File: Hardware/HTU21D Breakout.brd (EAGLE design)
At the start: 15.2 x 15.2 mm, 13 parts, among them U1 HTU21D

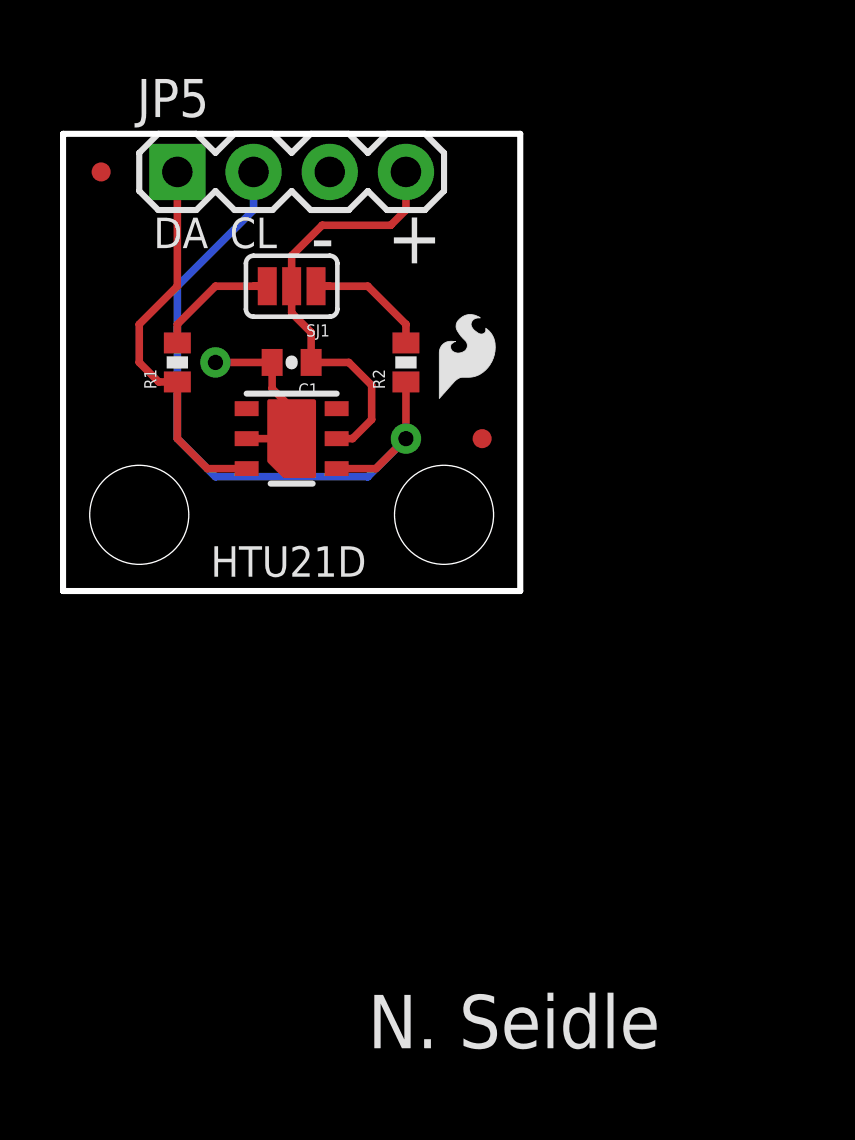
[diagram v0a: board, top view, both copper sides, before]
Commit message: Re-routing post review with engineering recommendations.
Moved to 0603 footprints. Removed ground planes to align with datasheet
thermal recommendations. Added OSHW logo. Updated frame to CC 3.0. Added
revision code to bottom copper.
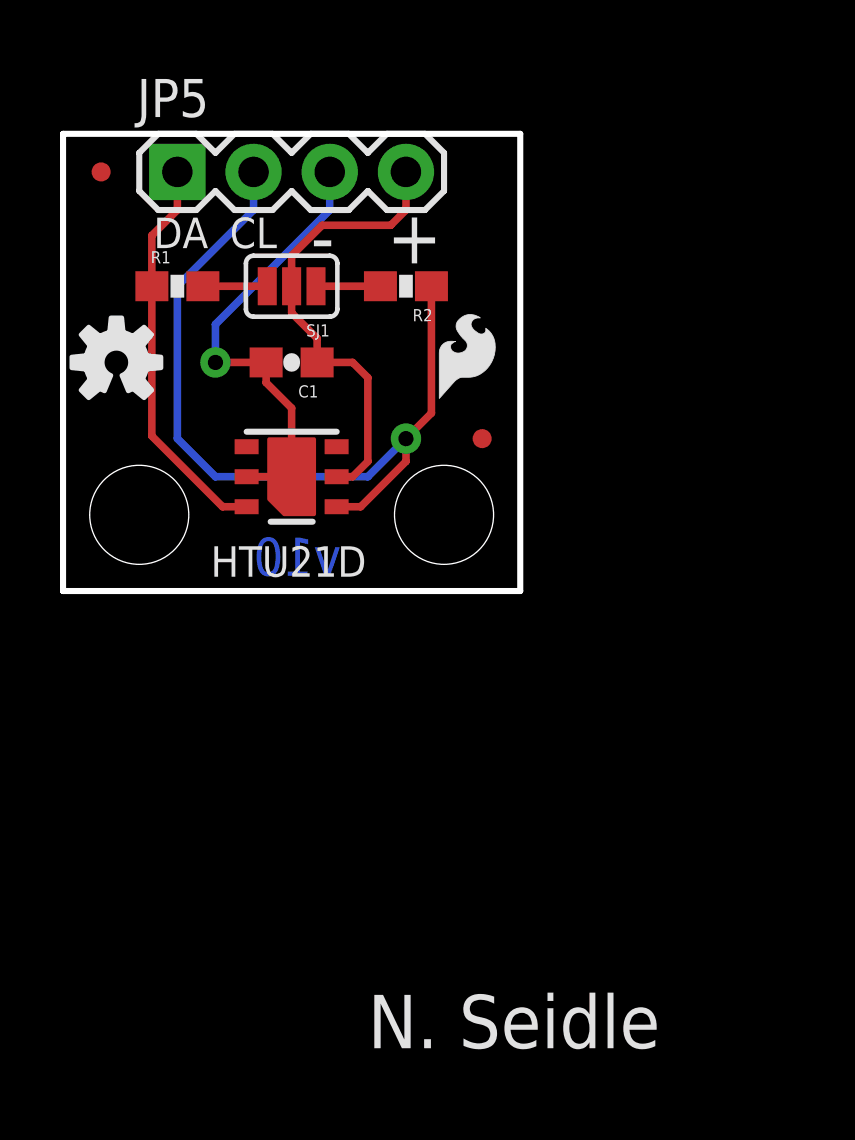
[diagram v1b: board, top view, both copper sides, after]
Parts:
- removed FRAME1: FRAME-LETTER, SparkFun-Aesthetics:CREATIVE_COMMONS
- added FRAME2: FRAME-LETTER, SparkFun-Aesthetics:CREATIVE_COMMONS
- added LOGO2: OSHW-LOGOS, SparkFun-Aesthetics:OSHW-LOGO-S
- C1: device SparkFun:0402-CAP -> SparkFun:0603-CAP
- R1, R2: device SparkFun:0402-RES -> SparkFun:0603-RES
- moved R1 2.54 mm to (3.81, 10.2), turned to 0 degrees
- moved R2 2.54 mm to (11.4, 10.2), turned to 180 degrees
- moved U1 1.27 mm to (7.62, 3.81)
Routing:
- net GND: track 6.20 -> 15.3 mm
- net SCL: track 23.2 -> 27.7 mm
- net N$1: track 4.60 -> 2.15 mm
- net N$2: track 4.60 -> 2.15 mm
- net 3.3V: track 14.4 -> 15.6 mm
- removed copper zone on layer 1, net GND
- removed copper zone on layer 16, net GND
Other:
- board text added: "v10"
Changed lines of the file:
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@@
 <?xml version="1.0" encoding="utf-8"?>
 <!DOCTYPE eagle SYSTEM "eagle.dtd">
-<eagle version="6.5.0">
+<eagle version="6.4">
 <drawing>
 <settings>
@@
 <text x="3.01625" y="11.43" size="1.016" layer="21" font="vector" ratio="15">DA</text>
 <text x="10.16" y="-15.24" size="1.778" layer="21">N. Seidle</text>
+<text x="9.271" y="0.508" size="1.27" layer="16" ratio="20" rot="MR0">v10</text>
 </plain>
 <attributes>
@@
 <elements>
 <element name="LOGO1" library="SparkFun" package="SFE-LOGO-FLAME" value="LOGO-SFESK" x="12.54125" y="6.4135"/>
-<element name="C1" library="SparkFun" package="0402-CAP" value="0.1uF" x="7.62" y="7.62" rot="R180"/>
-<element name="R1" library="SparkFun" package="0402-RES" value="4.7k" x="3.81" y="7.62" rot="R90"/>
-<element name="R2" library="SparkFun" package="0402-RES" value="4.7k" x="11.43" y="7.62" rot="R90"/>
+<element name="C1" library="SparkFun" package="0603-CAP" value="0.1uF" x="7.62" y="7.62" rot="R180"/>
+<element name="R1" library="SparkFun" package="0603-RES" value="4.7k" x="3.81" y="10.16"/>
+<element name="R2" library="SparkFun" package="0603-RES" value="4.7k" x="11.43" y="10.16" rot="R180"/>
 <element name="SJ1" library="mike-temp" package="SJ_3_PASTE1&amp;2&amp;3" value="" x="7.62" y="10.16" rot="R180"/>
 <element name="STANDOFF2" library="SparkFun-Electromechanical" package="STAND-OFF" value="STAND-OFF" x="2.54" y="2.54"/>
@@
 <element name="JP3" library="SparkFun-Aesthetics" package="MICRO-FIDUCIAL" value="FIDUCIALUFIDUCIAL" x="1.27" y="13.97"/>
 <element name="JP4" library="SparkFun-Aesthetics" package="MICRO-FIDUCIAL" value="FIDUCIALUFIDUCIAL" x="13.97" y="5.08"/>
-<element name="U1" library="SparkFun-Sensors" package="HTU21D" value="HTU21D" x="7.62" y="5.08"/>
-<element name="FRAME1" library="SparkFun-Aesthetics" package="CREATIVE_COMMONS" value="FRAME-LETTER" x="-22.6395375" y="-15.24"/>
+<element name="U1" library="SparkFun-Sensors" package="HTU21D" value="HTU21D" x="7.62" y="3.81"/>
 <element name="JP5" library="SparkFun-Connectors" package="1X04" value="" x="3.81" y="13.97"/>
+<element name="LOGO2" library="SparkFun-Aesthetics" package="OSHW-LOGO-S" value="OSHW-LOGOS" x="1.778" y="7.62"/>
+<element name="FRAME2" library="SparkFun-Aesthetics" package="CREATIVE_COMMONS" value="FRAME-LETTER" x="-21.59" y="-24.13"/>
 </elements>
 <signals>
 <signal name="GND">
 <contactref element="C1" pad="2"/>
-<polygon width="0.254" layer="1" isolate="0.254" orphans="yes">
-<vertex x="0" y="15.24"/>
-<vertex x="0" y="0"/>
-<vertex x="15.24" y="0"/>
-<vertex x="15.24" y="15.24"/>
-</polygon>
-<polygon width="0.254" layer="16" isolate="0.254" orphans="yes">
-<vertex x="0" y="15.24"/>
-<vertex x="0" y="0"/>
-<vertex x="15.24" y="0"/>
-<vertex x="15.24" y="15.24"/>
-</polygon>
 <contactref element="U1" pad="2"/>
 <contactref element="U1" pad="7"/>
@@
 <contactref element="U1" pad="2"/>
 <contactref element="JP5" pad="3"/>
-<wire x1="6.12" y1="5.08" x2="7.62" y2="5.08" width="0.254" layer="1"/>
-<wire x1="7.62" y1="5.08" x2="7.62" y2="6.096" width="0.254" layer="1"/>
-<wire x1="7.62" y1="6.096" x2="6.97" y2="6.746" width="0.254" layer="1"/>
-<wire x1="6.97" y1="7.62" x2="6.97" y2="6.746" width="0.254" layer="1"/>
-<wire x1="6.97" y1="7.62" x2="5.08" y2="7.62" width="0.254" layer="1"/>
+<wire x1="6.77" y1="7.62" x2="6.77" y2="6.946" width="0.254" layer="1"/>
 <via x="5.08" y="7.62" extent="1-16" drill="0.508"/>
+<wire x1="6.12" y1="3.81" x2="7.62" y2="3.81" width="0.254" layer="1"/>
+<wire x1="5.08" y1="7.62" x2="6.77" y2="7.62" width="0.254" layer="1"/>
+<wire x1="5.08" y1="8.89" x2="5.08" y2="7.62" width="0.254" layer="16"/>
+<wire x1="8.89" y1="13.97" x2="8.89" y2="12.7" width="0.254" layer="16"/>
+<wire x1="8.89" y1="12.7" x2="5.08" y2="8.89" width="0.254" layer="16"/>
+<wire x1="6.77" y1="6.946" x2="7.62" y2="6.096" width="0.254" layer="1"/>
+<wire x1="7.62" y1="6.096" x2="7.62" y2="3.81" width="0.254" layer="1"/>
 </signal>
 <signal name="SCL">
@@
 <contactref element="U1" pad="4"/>
 <contactref element="JP5" pad="2"/>
-<wire x1="9.12" y1="4.08" x2="10.43" y2="4.08" width="0.254" layer="1"/>
 <wire x1="6.35" y1="13.97" x2="6.35" y2="12.7" width="0.254" layer="16"/>
 <wire x1="6.35" y1="12.7" x2="3.81" y2="10.16" width="0.254" layer="16"/>
@@
 <wire x1="10.16" y1="3.81" x2="11.43" y2="5.08" width="0.254" layer="16"/>
 <via x="11.43" y="5.08" extent="1-16" drill="0.508"/>
-<wire x1="11.43" y1="6.97" x2="11.43" y2="5.08" width="0.254" layer="1"/>
-<wire x1="10.43" y1="4.08" x2="11.43" y2="5.08" width="0.254" layer="1"/>
+<wire x1="12.28" y1="10.16" x2="12.28" y2="5.93" width="0.254" layer="1"/>
+<wire x1="12.28" y1="5.93" x2="11.43" y2="5.08" width="0.254" layer="1"/>
+<wire x1="9.12" y1="2.81" x2="9.922" y2="2.81" width="0.254" layer="1"/>
+<wire x1="9.922" y1="2.81" x2="11.43" y2="4.318" width="0.254" layer="1"/>
+<wire x1="11.43" y1="4.318" x2="11.43" y2="5.08" width="0.254" layer="1"/>
 </signal>
 <signal name="SDA">
@@
 <contactref element="U1" pad="3"/>
 <contactref element="JP5" pad="1"/>
-<wire x1="6.12" y1="4.08" x2="4.81" y2="4.08" width="0.254" layer="1"/>
-<wire x1="3.81" y1="13.97" x2="3.81" y2="10.16" width="0.254" layer="1"/>
-<wire x1="3.81" y1="10.16" x2="2.54" y2="8.89" width="0.254" layer="1"/>
-<wire x1="2.54" y1="8.89" x2="2.54" y2="7.62" width="0.254" layer="1"/>
-<wire x1="3.81" y1="6.97" x2="3.19" y2="6.97" width="0.254" layer="1"/>
-<wire x1="3.19" y1="6.97" x2="2.54" y2="7.62" width="0.254" layer="1"/>
-<wire x1="3.81" y1="6.97" x2="3.81" y2="5.08" width="0.254" layer="1"/>
-<wire x1="4.81" y1="4.08" x2="3.81" y2="5.08" width="0.254" layer="1"/>
+<wire x1="2.96" y1="10.16" x2="2.96" y2="11.85" width="0.254" layer="1"/>
+<wire x1="2.96" y1="11.85" x2="3.81" y2="12.7" width="0.254" layer="1"/>
+<wire x1="3.81" y1="12.7" x2="3.81" y2="13.97" width="0.254" layer="1"/>
+<wire x1="2.96" y1="10.16" x2="2.96" y2="5.168" width="0.254" layer="1"/>
+<wire x1="6.12" y1="2.81" x2="5.318" y2="2.81" width="0.254" layer="1"/>
+<wire x1="5.318" y1="2.81" x2="2.96" y2="5.168" width="0.254" layer="1"/>
 </signal>
 <signal name="3.3V">
@@
 <contactref element="SJ1" pad="2"/>
 <contactref element="U1" pad="5"/>
-<wire x1="9.12" y1="5.08" x2="9.652" y2="5.08" width="0.254" layer="1"/>
-<wire x1="9.652" y1="5.08" x2="10.287" y2="5.715" width="0.254" layer="1"/>
-<wire x1="10.287" y1="5.715" x2="10.287" y2="6.858" width="0.254" layer="1"/>
-<wire x1="10.287" y1="6.858" x2="9.525" y2="7.62" width="0.254" layer="1"/>
-<wire x1="9.525" y1="7.62" x2="8.27" y2="7.62" width="0.254" layer="1"/>
-<wire x1="7.62" y1="10.16" x2="7.62" y2="9.271" width="0.254" layer="1"/>
-<wire x1="7.62" y1="9.271" x2="8.27" y2="8.621" width="0.254" layer="1"/>
-<wire x1="8.27" y1="7.62" x2="8.27" y2="8.621" width="0.254" layer="1"/>
 <wire x1="7.62" y1="10.16" x2="7.62" y2="11.176" width="0.254" layer="1"/>
 <wire x1="7.62" y1="11.176" x2="8.636" y2="12.192" width="0.254" layer="1"/>
@@
 <contactref element="JP5" pad="4"/>
 <wire x1="11.43" y1="13.97" x2="11.43" y2="12.7" width="0.254" layer="1"/>
+<wire x1="7.62" y1="10.16" x2="7.62" y2="9.271" width="0.254" layer="1"/>
+<wire x1="7.62" y1="9.271" x2="8.47" y2="8.421" width="0.254" layer="1"/>
+<wire x1="8.47" y1="7.62" x2="8.47" y2="8.421" width="0.254" layer="1"/>
+<wire x1="9.12" y1="3.81" x2="9.652" y2="3.81" width="0.254" layer="1"/>
+<wire x1="9.652" y1="3.81" x2="10.16" y2="4.318" width="0.254" layer="1"/>
+<wire x1="10.16" y1="4.318" x2="10.16" y2="7.112" width="0.254" layer="1"/>
+<wire x1="8.47" y1="7.62" x2="9.652" y2="7.62" width="0.254" layer="1"/>
+<wire x1="9.652" y1="7.62" x2="10.16" y2="7.112" width="0.254" layer="1"/>
 </signal>
 <signal name="N$1">
 <contactref element="R1" pad="2"/>
 <contactref element="SJ1" pad="3"/>
-<wire x1="6.8072" y1="10.16" x2="6.35" y2="10.16" width="0.254" layer="1"/>
-<wire x1="3.81" y1="8.89" x2="3.81" y2="8.27" width="0.254" layer="1"/>
-<wire x1="3.81" y1="8.89" x2="5.08" y2="10.16" width="0.254" layer="1"/>
-<wire x1="5.08" y1="10.16" x2="6.8072" y2="10.16" width="0.254" layer="1"/>
+<wire x1="4.66" y1="10.16" x2="6.8072" y2="10.16" width="0.254" layer="1"/>
 </signal>
 <signal name="N$2">
 <contactref element="R2" pad="2"/>
 <contactref element="SJ1" pad="1"/>
-<wire x1="8.4328" y1="10.16" x2="8.89" y2="10.16" width="0.254" layer="1"/>
-<wire x1="11.43" y1="8.89" x2="11.43" y2="8.27" width="0.254" layer="1"/>
-<wire x1="11.43" y1="8.89" x2="10.16" y2="10.16" width="0.254" layer="1"/>
-<wire x1="10.16" y1="10.16" x2="8.4328" y2="10.16" width="0.254" layer="1"/>
+<wire x1="8.4328" y1="10.16" x2="10.58" y2="10.16" width="0.254" layer="1"/>
 </signal>
 </signals>

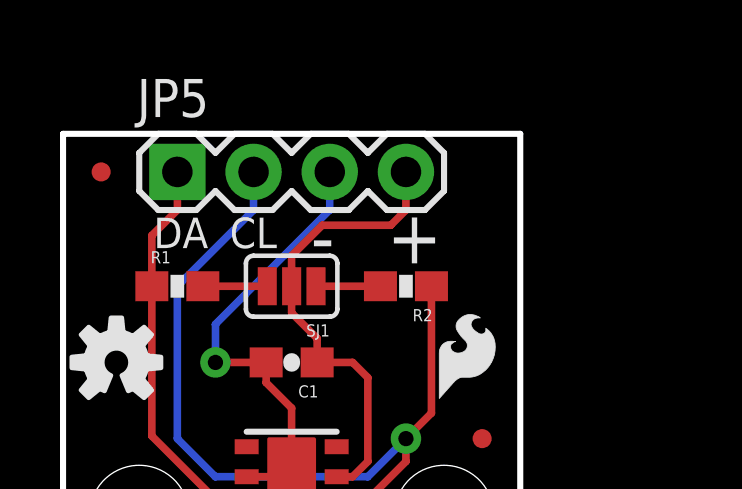
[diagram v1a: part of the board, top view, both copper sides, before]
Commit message: Added flags on data lines to schematic.
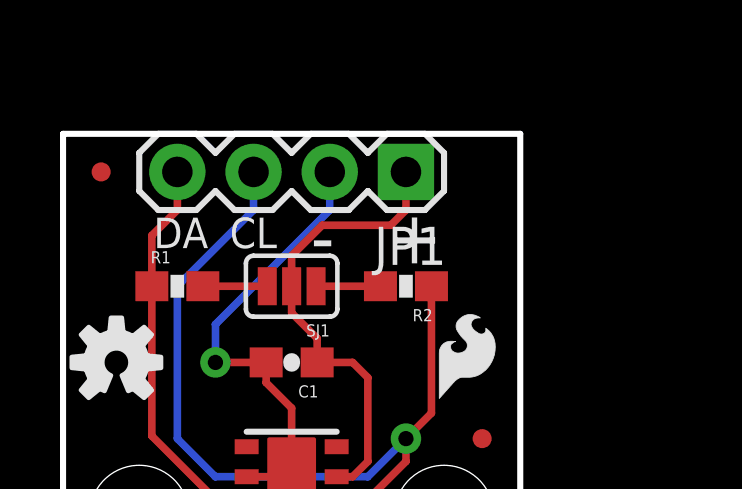
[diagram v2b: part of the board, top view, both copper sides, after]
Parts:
- removed JP5: (no value), SparkFun-Connectors:1X04
- added JP1: (no value), SparkFun-Connectors:1X04
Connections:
- net 3.3V: now also JP1.1; no longer JP5.4
- net GND: now also JP1.2; no longer JP5.3
- net SCL: now also JP1.3; no longer JP5.2
- net SDA: now also JP1.4; no longer JP5.1
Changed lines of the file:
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@@
 <layer number="19" name="Unrouted" color="6" fill="1" visible="yes" active="yes"/>
 <layer number="20" name="Dimension" color="6" fill="1" visible="yes" active="yes"/>
-<layer number="21" name="tPlace" color="15" fill="1" visible="yes" active="yes"/>
-<layer number="22" name="bPlace" color="6" fill="1" visible="yes" active="yes"/>
+<layer number="21" name="tPlace" color="16" fill="1" visible="yes" active="yes"/>
+<layer number="22" name="bPlace" color="14" fill="1" visible="yes" active="yes"/>
 <layer number="23" name="tOrigins" color="15" fill="1" visible="yes" active="yes"/>
 <layer number="24" name="bOrigins" color="15" fill="1" visible="yes" active="yes"/>
@@
 <element name="JP4" library="SparkFun-Aesthetics" package="MICRO-FIDUCIAL" value="FIDUCIALUFIDUCIAL" x="13.97" y="5.08"/>
 <element name="U1" library="SparkFun-Sensors" package="HTU21D" value="HTU21D" x="7.62" y="3.81"/>
-<element name="JP5" library="SparkFun-Connectors" package="1X04" value="" x="3.81" y="13.97"/>
 <element name="LOGO2" library="SparkFun-Aesthetics" package="OSHW-LOGO-S" value="OSHW-LOGOS" x="1.778" y="7.62"/>
 <element name="FRAME2" library="SparkFun-Aesthetics" package="CREATIVE_COMMONS" value="FRAME-LETTER" x="-21.59" y="-24.13"/>
+<element name="JP1" library="SparkFun-Connectors" package="1X04" value="" x="11.43" y="13.97" rot="R180"/>
 </elements>
 <signals>
@@
 <contactref element="U1" pad="7"/>
 <contactref element="U1" pad="2"/>
-<contactref element="JP5" pad="3"/>
 <wire x1="6.77" y1="7.62" x2="6.77" y2="6.946" width="0.254" layer="1"/>
 <via x="5.08" y="7.62" extent="1-16" drill="0.508"/>
@@
 <wire x1="5.08" y1="7.62" x2="6.77" y2="7.62" width="0.254" layer="1"/>
 <wire x1="5.08" y1="8.89" x2="5.08" y2="7.62" width="0.254" layer="16"/>
-<wire x1="8.89" y1="13.97" x2="8.89" y2="12.7" width="0.254" layer="16"/>
 <wire x1="8.89" y1="12.7" x2="5.08" y2="8.89" width="0.254" layer="16"/>
 <wire x1="6.77" y1="6.946" x2="7.62" y2="6.096" width="0.254" layer="1"/>
 <wire x1="7.62" y1="6.096" x2="7.62" y2="3.81" width="0.254" layer="1"/>
+<contactref element="JP1" pad="2"/>
+<wire x1="8.89" y1="13.97" x2="8.89" y2="12.7" width="0.254" layer="16"/>
 </signal>
 <signal name="SCL">
 <contactref element="R2" pad="1"/>
 <contactref element="U1" pad="4"/>
-<contactref element="JP5" pad="2"/>
-<wire x1="6.35" y1="13.97" x2="6.35" y2="12.7" width="0.254" layer="16"/>
 <wire x1="6.35" y1="12.7" x2="3.81" y2="10.16" width="0.254" layer="16"/>
 <wire x1="3.81" y1="10.16" x2="3.81" y2="5.08" width="0.254" layer="16"/>
@@
 <wire x1="9.922" y1="2.81" x2="11.43" y2="4.318" width="0.254" layer="1"/>
 <wire x1="11.43" y1="4.318" x2="11.43" y2="5.08" width="0.254" layer="1"/>
+<contactref element="JP1" pad="3"/>
+<wire x1="6.35" y1="13.97" x2="6.35" y2="12.7" width="0.254" layer="16"/>
 </signal>
 <signal name="SDA">
 <contactref element="R1" pad="1"/>
 <contactref element="U1" pad="3"/>
-<contactref element="JP5" pad="1"/>
 <wire x1="2.96" y1="10.16" x2="2.96" y2="11.85" width="0.254" layer="1"/>
 <wire x1="2.96" y1="11.85" x2="3.81" y2="12.7" width="0.254" layer="1"/>
-<wire x1="3.81" y1="12.7" x2="3.81" y2="13.97" width="0.254" layer="1"/>
 <wire x1="2.96" y1="10.16" x2="2.96" y2="5.168" width="0.254" layer="1"/>
 <wire x1="6.12" y1="2.81" x2="5.318" y2="2.81" width="0.254" layer="1"/>
 <wire x1="5.318" y1="2.81" x2="2.96" y2="5.168" width="0.254" layer="1"/>
+<contactref element="JP1" pad="4"/>
+<wire x1="3.81" y1="13.97" x2="3.81" y2="12.7" width="0.254" layer="1"/>
 </signal>
 <signal name="3.3V">
@@
 <wire x1="8.636" y1="12.192" x2="10.922" y2="12.192" width="0.254" layer="1"/>
 <wire x1="10.922" y1="12.192" x2="11.43" y2="12.7" width="0.254" layer="1"/>
-<contactref element="JP5" pad="4"/>
-<wire x1="11.43" y1="13.97" x2="11.43" y2="12.7" width="0.254" layer="1"/>
 <wire x1="7.62" y1="10.16" x2="7.62" y2="9.271" width="0.254" layer="1"/>
 <wire x1="7.62" y1="9.271" x2="8.47" y2="8.421" width="0.254" layer="1"/>
@@
 <wire x1="8.47" y1="7.62" x2="9.652" y2="7.62" width="0.254" layer="1"/>
 <wire x1="9.652" y1="7.62" x2="10.16" y2="7.112" width="0.254" layer="1"/>
+<contactref element="JP1" pad="1"/>
+<wire x1="11.43" y1="13.97" x2="11.43" y2="12.7" width="0.254" layer="1"/>
 </signal>
 <signal name="N$1">

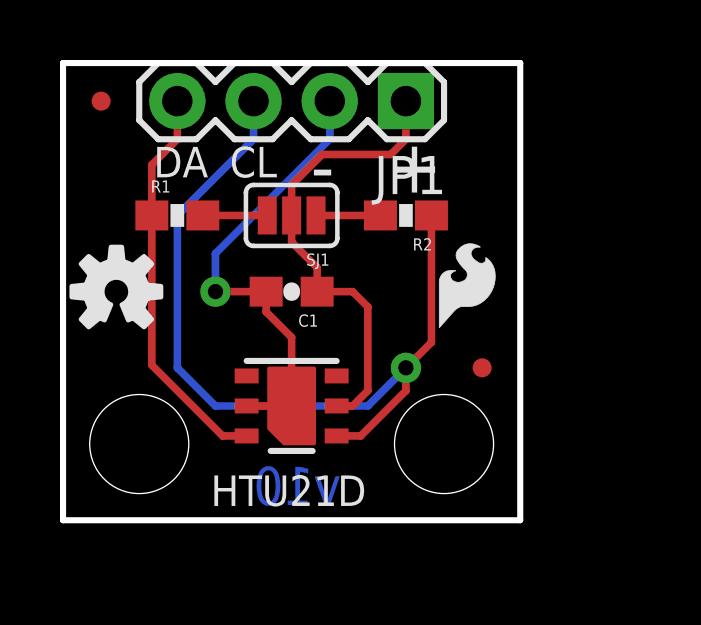
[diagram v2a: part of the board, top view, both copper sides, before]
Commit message: Corrected a reversed the footprint.
Arg! I forgot to invert the footprint. Corrected.
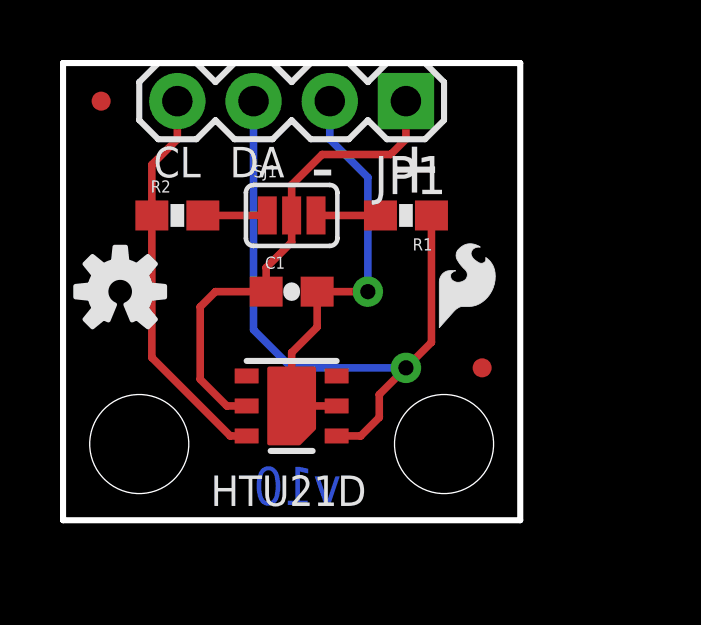
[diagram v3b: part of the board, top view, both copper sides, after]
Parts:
- moved R1 7.62 mm to (11.4, 10.2), turned to 180 degrees
- moved R2 7.62 mm to (3.81, 10.2), turned to 0 degrees
- moved LOGO2 0.13 mm to (1.91, 7.62)
- turned C1 to 0 degrees
- turned SJ1 to 0 degrees
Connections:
- net 3.3V: now also U1.VDD; no longer U1.5
- net GND: now also U1.GND; no longer U1.2
- net SCL: now also JP1.4, U1.SCK; no longer JP1.3, U1.4
- net SDA: now also JP1.3, U1.DATA; no longer JP1.4, U1.3
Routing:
- net SCL: track 27.7 -> 13.1 mm, vias 1 -> 0
- net SDA: track 13.3 -> 22.4 mm, vias 0 -> 1
- net GND: track 15.3 -> 14.2 mm
- net 3.3V: track 15.6 -> 16.4 mm
